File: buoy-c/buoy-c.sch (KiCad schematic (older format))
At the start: 91 parts, among them J1 UJ31-CH-G2-SMT-TR, J10 Conn_01x06_Male, J11 TERM-BLK-2P, J14 Conn_01x09_Male, J2 BAT-HLD-001-THM, J3 Conn_01x02_Male, J4 U.FL-R-SMT-1_10_, J5 BH-18650-PC, J7 Conn_01x02_Male, J8 Conn_01x03_Male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

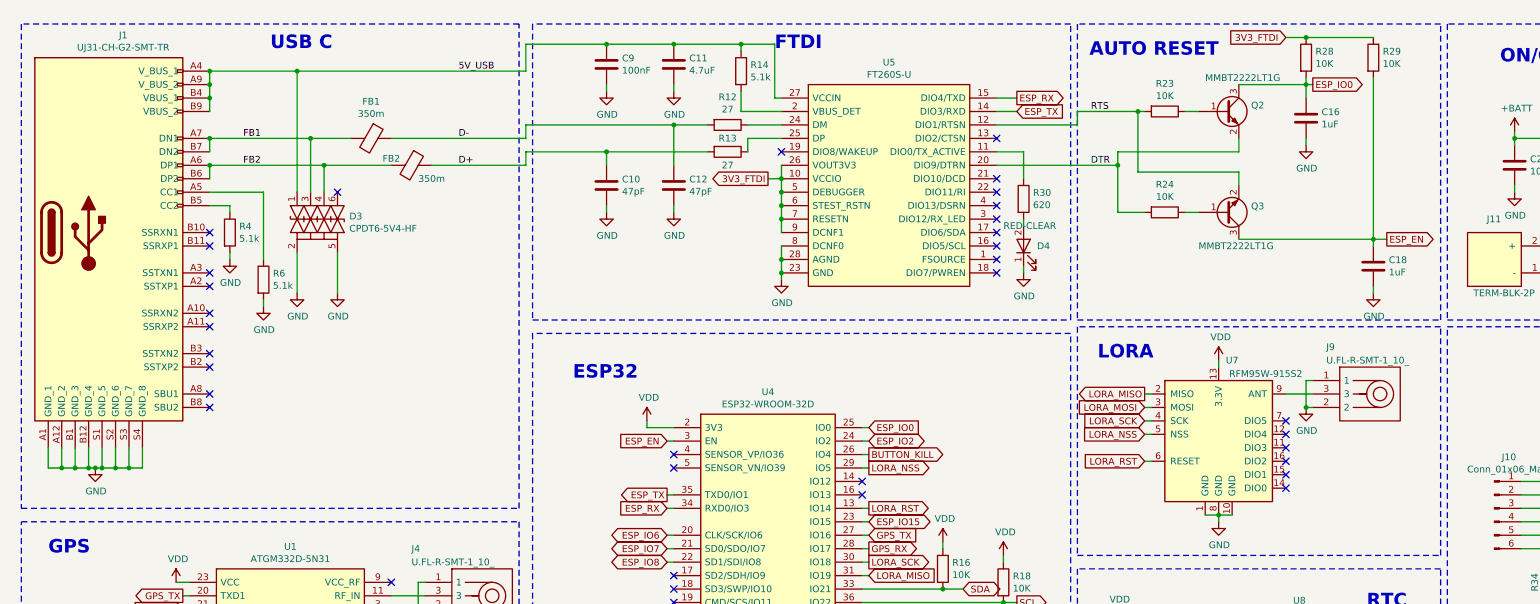
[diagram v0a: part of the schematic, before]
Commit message: Removed FTDI and added extra headers
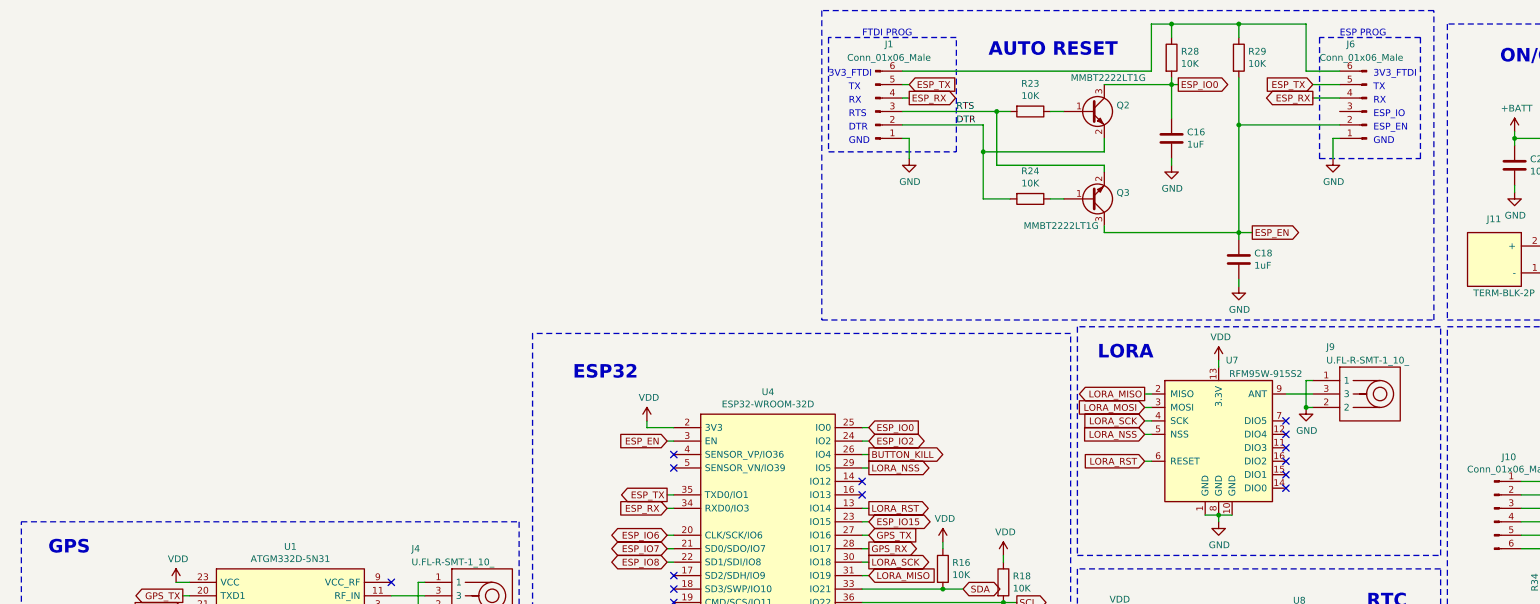
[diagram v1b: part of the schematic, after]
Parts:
- removed C10, C12: 47pF, Capacitor_SMD:C_0805_2012Metric, symbol C-47pF-0805:47pF
- removed C11: 4.7uF, Capacitor_SMD:C_0805_2012Metric, symbol C-4.7uF-0805:4.7uF
- removed C9: 100nF, Capacitor_SMD:C_0805_2012Metric, symbol C-100nF-0805:100nF
- removed D3: CPDT6-5V4-HF, Package_TO_SOT_SMD:SOT-23-6_Handsoldering, symbol CPDT6-5V4-HF:CPDT6-5V4-HF
- removed D4: RED-CLEAR, LED_SMD:LED_0805_2012Metric, symbol LED-RED-CLEAR-0805:RED-CLEAR
- removed FB1, FB2: 350m, Resistor_SMD:R_0805_2012Metric, symbol FB-350m-300mA-0805:350m
- removed J1: UJ31-CH-G2-SMT-TR, UJ31CHG2SMTTR:UJ31CHG2SMTTR, symbol UJ31-CH-G2-SMT-TR:UJ31-CH-G2-SMT-TR
- removed R12, R13: 27, Resistor_SMD:R_0805_2012Metric, symbol R-27-0805:27
- removed R14, R4, R6: 5.1k, Resistor_SMD:R_0805_2012Metric, symbol R-5.1k-0805:5.1k
- removed R30: 620, Resistor_SMD:R_0805_2012Metric, symbol R-620-0805:620
- removed U5: FT260S-U, Package_SO:TSSOP-28_4.4x9.7mm_P0.65mm, symbol FT260S-U:FT260S-U
- added J1, J6: Conn_01x06_Male, Connector_PinHeader_2.54mm:PinHeader_1x06_P2.54mm_Vertical, symbol Connector:Conn_01x06_Male
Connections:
- net DTR: now also J1.2 (Pin_2)
- net ESP_EN: now also J6.2 (Pin_2)
- net ESP_RX: now also J1.4 (Pin_4), J6.4 (Pin_4)
- net ESP_TX: now also J1.5 (Pin_5), J6.5 (Pin_5)
- net GND: now also J1.1 (Pin_1), J6.1 (Pin_1)
- net RTS: now also J1.3 (Pin_3)
- net 3V3_FTDI: no longer names the net of R28.1, R29.1
- net 3V3_FTDI: now also J1.6 (Pin_6), J6.6 (Pin_6)
- no-connect marks 66 -> 45
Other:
- note added: "3V3_FTDI"
- note added: "DTR"
- note added: "ESP PROG"
- note added: "ESP_EN"
- note added: "ESP_IO"
- note added: "FTDI PROG"
- note added: "GND"
- note added: "RTS"
- note added: "RX"
- note added: "TX"
- note removed: "FTDI"
- note removed: "USB C"
- moved on the sheet: C16, C18, Q2, Q3, R23, R24, R28, R29

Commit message: Re routed Sepic converter
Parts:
- removed J14: Conn_01x09_Male, Connector_PinHeader_2.54mm:PinHeader_1x09_P2.54mm_Vertical, symbol Connector:Conn_01x09_Male
- removed R33: 0, Resistor_SMD:R_0805_2012Metric, symbol R-0-0805:0
- added J12: Conn_01x04_Male, Connector_PinHeader_2.54mm:PinHeader_1x04_P2.54mm_Vertical, symbol Connector:Conn_01x04_Male
- added R4, R6: 100k, Resistor_SMD:R_0805_2012Metric_Pad1.20x1.40mm_HandSolder, symbol R-100k-0805:100k
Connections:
- net ESP_EN: now also R4.2
- net ESP_IO0: now also R6.2
- net GND: now also J12.1 (Pin_1)
- net SCL: now also J12.3 (Pin_3)
- net SDA: now also J12.2 (Pin_2)
- net VDD: now also J12.4 (Pin_4), R4.1, R6.1
- no-connect marks 45 -> 40
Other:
- note removed: "Solder R32 to connect VDD to 3V3\nSolder R33 to connect VDD to BATT\nDO NOT SOLDER R32 AND R33\nIT WILL CREATE A SHORT CIRCUIT\nBETWEEN BATT AND 3V3"
- note removed: "VDD Selector"
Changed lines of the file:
@@
 	1    0    0    -1
 $EndComp
-Text GLabel 5750 4000 0    50   Input ~ 0
+Text GLabel 5700 4000 0    50   Input ~ 0
 ESP_EN
 Text GLabel 5750 4400 0    50   Output ~ 0
@@
 Text GLabel 7250 3900 2    50   Input ~ 0
 ESP_IO0
-Wire Wire Line
-	5750 4000 5800 4000
 Wire Wire Line
 	5750 4400 5800 4400
@@
 Wire Wire Line
 	5600 3850 5600 3900
-Wire Wire Line
-	5600 3900 5800 3900
 Wire Wire Line
 	9850 3400 9850 3450
@@
 $EndComp
 $Comp
-L power:+BATT #PWR0134
-U 1 1 616C8CB2
-P 6050 8950
-F 0 "#PWR0134" H 6050 8800 50  0001 C CNN
-F 1 "+BATT" H 6065 9123 50  0000 C CNN
-F 2 "" H 6050 8950 50  0001 C CNN
-F 3 "" H 6050 8950 50  0001 C CNN
-	1    6050 8950
-	1    0    0    -1
-$EndComp
-$Comp
 L power:VDD #PWR0135
 U 1 1 6171CAF7
@@
 	1    0    0    -1
 $EndComp
-Text Notes 5150 8650 0    50   ~ 0
-VDD Selector
 $Comp
 L power:VDD #PWR0136
@@
 	1    0    0    -1
 $EndComp
-Text Notes 5050 9650 0    50   ~ 0
-Solder R32 to connect VDD to 3V3\nSolder R33 to connect VDD to BATT\nDO NOT SOLDER R32 AND R33\nIT WILL CREATE A SHORT CIRCUIT\nBETWEEN BATT AND 3V3
 Connection ~ 3700 9000
 Connection ~ 4750 9000
@@
 Text Notes 8800 9400 0    100  ~ 20
 BATT\nLEVEL
-NoConn ~ 10300 9650
-NoConn ~ 10300 10250
-NoConn ~ 10300 10350
-NoConn ~ 10300 10050
-NoConn ~ 10300 10150
 $Comp
 L power:GND #PWR0163
 U 1 1 61E1DC37
-P 10000 9800
-F 0 "#PWR0163" H 10000 9550 50  0001 C CNN
-F 1 "GND" H 10005 9627 50  0000 C CNN
-F 2 "" H 10000 9800 50  0001 C CNN
-F 3 "" H 10000 9800 50  0001 C CNN
-	1    10000 9800
-	1    0    0    -1
-$EndComp
-Text GLabel 10300 9950 0    50   BiDi ~ 0
+P 10300 9850
+F 0 "#PWR0163" H 10300 9600 50  0001 C CNN
+F 1 "GND" H 10305 9677 50  0000 C CNN
+F 2 "" H 10300 9850 50  0001 C CNN
+F 3 "" H 10300 9850 50  0001 C CNN
+	1    10300 9850
+	1    0    0    -1
+$EndComp
+Text GLabel 10300 9750 0    50   BiDi ~ 0
 SDA
-Text GLabel 10300 9850 0    50   BiDi ~ 0
+Text GLabel 10300 9650 0    50   BiDi ~ 0
 SCL
 Wire Notes Line style solid
@@
 BATT
 $Comp
-L Connector:Conn_01x09_Male J14
-U 1 1 61305654
-P 10500 9950
-F 0 "J14" H 10600 9300 50  0000 R CNN
-F 1 "Conn_01x09_Male" H 10600 9400 50  0000 R CNN
-F 2 "Connector_PinHeader_2.54mm:PinHeader_1x09_P2.54mm_Vertical" H 10500 9950 50  0001 C CNN
-F 3 "~" H 10500 9950 50  0001 C CNN
-	1    10500 9950
-	-1   0    0    1
-$EndComp
-$Comp
 L power:VDD #PWR0162
 U 1 1 61D5D079
@@
 Wire Wire Line
 	10200 9500 10200 9550
-Wire Wire Line
-	10200 9550 10300 9550
-Wire Wire Line
-	10000 9800 10000 9750
-Wire Wire Line
-	10000 9750 10300 9750
 Wire Wire Line
 	8250 4850 8250 4900
@@
 	0    1    1    0
 $EndComp
-$Comp
-L R-0-0805:0 R33
-U 1 1 617769B4
-P 5850 9000
-F 0 "R33" V 5643 9000 50  0000 C CNN
-F 1 "0" V 5734 9000 50  0000 C CNN
-F 2 "Resistor_SMD:R_0805_2012Metric" H 6750 8800 50  0001 C CNN
-F 3 "https://www.yageo.com/upload/media/product/productsearch/datasheet/rchip/PYu-RC_Group_51_RoHS_L_11.pdf" H 5850 9000 50  0001 C CNN
-F 4 "Digi-Key" H 6300 9000 50  0001 C CNN "Supplier 1"
-F 5 "311-0.0ARCT-ND" H 6450 8900 50  0001 C CNN "Supplier Part Number 1"
-F 6 "Yageo" H 6200 9250 50  0001 C CNN "Manufacturer"
-F 7 "RC0805JR-070RL" H 6450 9150 50  0001 C CNN "Manufacturer Part Number"
-	1    5850 9000
-	0    1    1    0
-$EndComp
-Wire Wire Line
-	5700 9000 5600 9000
 Wire Wire Line
 	5600 8950 5600 9000
-Connection ~ 5600 9000
 Wire Wire Line
 	5600 9000 5500 9000
-Wire Wire Line
-	6050 8950 6050 9000
-Wire Wire Line
-	6050 9000 6000 9000
 $Comp
 L power:GND #PWR0174
@@
 Wire Notes Line style solid
 	11450 3100 11450 800
+$Comp
+L R-100k-0805:100k R4
+U 1 1 62136266
+P 5750 3650
+F 0 "R4" H 5820 3696 50  0000 L CNN
+F 1 "100k" H 5820 3605 50  0000 L CNN
+F 2 "Resistor_SMD:R_0805_2012Metric_Pad1.20x1.40mm_HandSolder" H 7250 3900 50  0001 C CNN
+F 3 "https://www.seielect.com/catalog/sei-rmcf_rmcp.pdf" H 5750 3650 50  0001 C CNN
+F 4 "Digi-Key" H 6200 3800 50  0001 C CNN "Supplier 1"
+F 5 "RMCF0805FG100KCT-ND" H 6900 3800 50  0001 C CNN "Supplier Part Number 1"
+F 6 "Stackpole Electronics Inc" H 6500 3700 50  0001 C CNN "Manufacturer_Name"
+F 7 "RMCF0805FG100K" H 6350 3600 50  0001 C CNN "Manufacturer_Part_Number"
+	1    5750 3650
+	1    0    0    -1
+$EndComp
+$Comp
+L R-100k-0805:100k R6
+U 1 1 6213726D
+P 7200 3650
+F 0 "R6" H 7270 3696 50  0000 L CNN
+F 1 "100k" H 7270 3605 50  0000 L CNN
+F 2 "Resistor_SMD:R_0805_2012Metric_Pad1.20x1.40mm_HandSolder" H 8700 3900 50  0001 C CNN
+F 3 "https://www.seielect.com/catalog/sei-rmcf_rmcp.pdf" H 7200 3650 50  0001 C CNN
+F 4 "Digi-Key" H 7650 3800 50  0001 C CNN "Supplier 1"
+F 5 "RMCF0805FG100KCT-ND" H 8350 3800 50  0001 C CNN "Supplier Part Number 1"
+F 6 "Stackpole Electronics Inc" H 7950 3700 50  0001 C CNN "Manufacturer_Name"
+F 7 "RMCF0805FG100K" H 7800 3600 50  0001 C CNN "Manufacturer_Part_Number"
+	1    7200 3650
+	1    0    0    -1
+$EndComp
+$Comp
+L power:VDD #PWR0103
+U 1 1 6213EA4E
+P 5750 3450
+F 0 "#PWR0103" H 5750 3300 50  0001 C CNN
+F 1 "VDD" H 5765 3623 50  0000 C CNN
+F 2 "" H 5750 3450 50  0001 C CNN
+F 3 "" H 5750 3450 50  0001 C CNN
+	1    5750 3450
+	1    0    0    -1
+$EndComp
+$Comp
+L power:VDD #PWR0104
+U 1 1 6215D04A
+P 7200 3450
+F 0 "#PWR0104" H 7200 3300 50  0001 C CNN
+F 1 "VDD" H 7215 3623 50  0000 C CNN
+F 2 "" H 7200 3450 50  0001 C CNN
+F 3 "" H 7200 3450 50  0001 C CNN
+	1    7200 3450
+	1    0    0    -1
+$EndComp
+Wire Wire Line
+	7200 3900 7200 3800
+Connection ~ 7200 3900
+Wire Wire Line
+	7200 3450 7200 3500
+Wire Wire Line
+	5750 3500 5750 3450
+Wire Wire Line
+	5600 3900 5800 3900
+Wire Wire Line
+	5700 4000 5750 4000
+Wire Wire Line
+	5750 3800 5750 4000
+Connection ~ 5750 4000
+Wire Wire Line
+	5750 4000 5800 4000
+$Comp
+L Connector:Conn_01x04_Male J12
+U 1 1 622D640C
+P 10550 9750
+F 0 "J12" H 10600 9350 50  0000 R CNN
+F 1 "Conn_01x04_Male" H 10800 9450 50  0000 R CNN
+F 2 "Connector_PinHeader_2.54mm:PinHeader_1x04_P2.54mm_Vertical" H 10550 9750 50  0001 C CNN
+F 3 "~" H 10550 9750 50  0001 C CNN
+	1    10550 9750
+	-1   0    0    1
+$EndComp
+Wire Wire Line
+	10200 9550 10350 9550
+Wire Wire Line
+	10300 9650 10350 9650
+Wire Wire Line
+	10300 9750 10350 9750
+Wire Wire Line
+	10300 9850 10350 9850
 $EndSCHEMATC

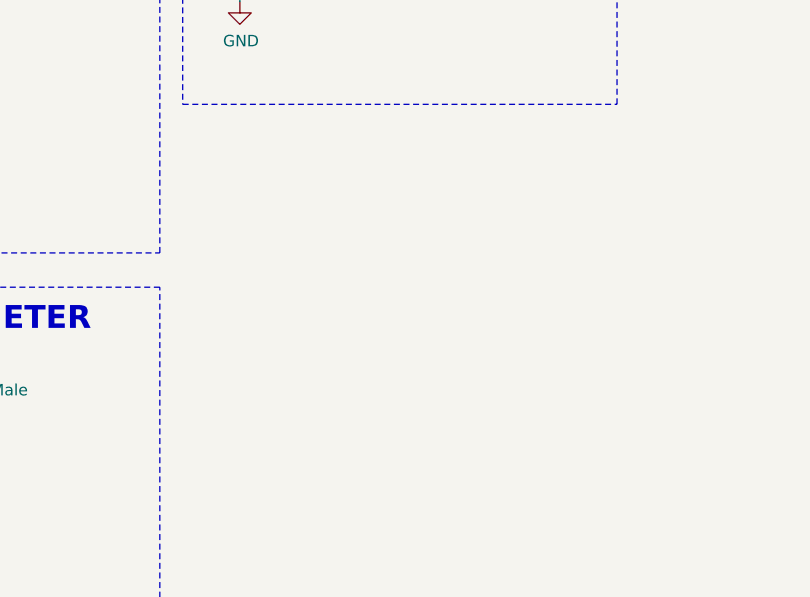
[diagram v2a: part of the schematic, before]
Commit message: Changed routing of the sepic converter
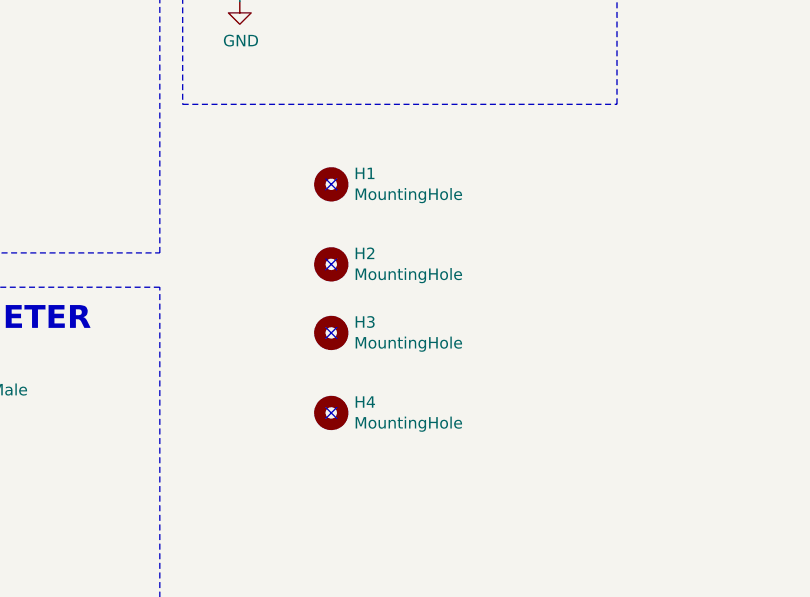
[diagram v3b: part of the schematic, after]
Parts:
- added H1, H2, H3, H4: MountingHole, MountingHole:MountingHole_3.5mm, symbol Mechanical:MountingHole
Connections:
- no-connect marks 40 -> 44
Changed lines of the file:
@@
 Wire Wire Line
 	10300 9850 10350 9850
+$Comp
+L Mechanical:MountingHole H2
+U 1 1 62149BD5
+P 12250 8900
+F 0 "H2" H 12350 8946 50  0000 L CNN
+F 1 "MountingHole" H 12350 8855 50  0000 L CNN
+F 2 "MountingHole:MountingHole_3.5mm" H 12250 8900 50  0001 C CNN
+F 3 "~" H 12250 8900 50  0001 C CNN
+	1    12250 8900
+	1    0    0    -1
+$EndComp
+$Comp
+L Mechanical:MountingHole H3
+U 1 1 6214C3F0
+P 12250 9200
+F 0 "H3" H 12350 9246 50  0000 L CNN
+F 1 "MountingHole" H 12350 9155 50  0000 L CNN
+F 2 "MountingHole:MountingHole_3.5mm" H 12250 9200 50  0001 C CNN
+F 3 "~" H 12250 9200 50  0001 C CNN
+	1    12250 9200
+	1    0    0    -1
+$EndComp
+$Comp
+L Mechanical:MountingHole H1
+U 1 1 6214D8CC
+P 12250 8550
+F 0 "H1" H 12350 8596 50  0000 L CNN
+F 1 "MountingHole" H 12350 8505 50  0000 L CNN
+F 2 "MountingHole:MountingHole_3.5mm" H 12250 8550 50  0001 C CNN
+F 3 "~" H 12250 8550 50  0001 C CNN
+	1    12250 8550
+	1    0    0    -1
+$EndComp
+$Comp
+L Mechanical:MountingHole H4
+U 1 1 6214E616
+P 12250 9550
+F 0 "H4" H 12350 9596 50  0000 L CNN
+F 1 "MountingHole" H 12350 9505 50  0000 L CNN
+F 2 "MountingHole:MountingHole_3.5mm" H 12250 9550 50  0001 C CNN
+F 3 "~" H 12250 9550 50  0001 C CNN
+	1    12250 9550
+	1    0    0    -1
+$EndComp
+NoConn ~ 12250 8550
+NoConn ~ 12250 8900
+NoConn ~ 12250 9200
+NoConn ~ 12250 9550
 $EndSCHEMATC
